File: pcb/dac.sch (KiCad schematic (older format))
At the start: 68 parts, among them U7 MAX5853ETL-T, U8 TLV3542IDR

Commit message: clean up ERC, more DFT stuff, started sigma delta adc
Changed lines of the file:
@@
 $Descr A4 11693 8268
 encoding utf-8
-Sheet 4 6
+Sheet 4 7
 Title ""
 Date ""
@@
 Connection ~ 10550 900
 Wire Wire Line
-	10550 900  10400 900
+	10550 900  10450 900
 $Comp
 L Connector:TestPoint TP27
@@
 Connection ~ 10550 1750
 Wire Wire Line
-	10550 1750 10400 1750
+	10550 1750 10450 1750
 $Comp
 L Connector:TestPoint TP28
@@
 Connection ~ 10550 2600
 Wire Wire Line
-	10550 2600 10400 2600
+	10550 2600 10450 2600
 $Comp
 L Connector:TestPoint TP22
@@
 Wire Bus Line
 	2450 2250 2450 3350
+$Comp
+L power:PWR_FLAG #FLG0106
+U 1 1 604F650D
+P 10450 2600
+F 0 "#FLG0106" H 10450 2675 50  0001 C CNN
+F 1 "PWR_FLAG" H 10450 2773 50  0000 C CNN
+F 2 "" H 10450 2600 50  0001 C CNN
+F 3 "~" H 10450 2600 50  0001 C CNN
+	1    10450 2600
+	1    0    0    -1
+$EndComp
+Connection ~ 10450 2600
+Wire Wire Line
+	10450 2600 10400 2600
+$Comp
+L power:PWR_FLAG #FLG0107
+U 1 1 604F7845
+P 10450 1750
+F 0 "#FLG0107" H 10450 1825 50  0001 C CNN
+F 1 "PWR_FLAG" H 10450 1923 50  0000 C CNN
+F 2 "" H 10450 1750 50  0001 C CNN
+F 3 "~" H 10450 1750 50  0001 C CNN
+	1    10450 1750
+	1    0    0    -1
+$EndComp
+Connection ~ 10450 1750
+Wire Wire Line
+	10450 1750 10400 1750
+$Comp
+L power:PWR_FLAG #FLG0108
+U 1 1 604F7E56
+P 10450 900
+F 0 "#FLG0108" H 10450 975 50  0001 C CNN
+F 1 "PWR_FLAG" H 10450 1073 50  0000 C CNN
+F 2 "" H 10450 900 50  0001 C CNN
+F 3 "~" H 10450 900 50  0001 C CNN
+	1    10450 900
+	1    0    0    -1
+$EndComp
+Connection ~ 10450 900
+Wire Wire Line
+	10450 900  10400 900
 $EndSCHEMATC

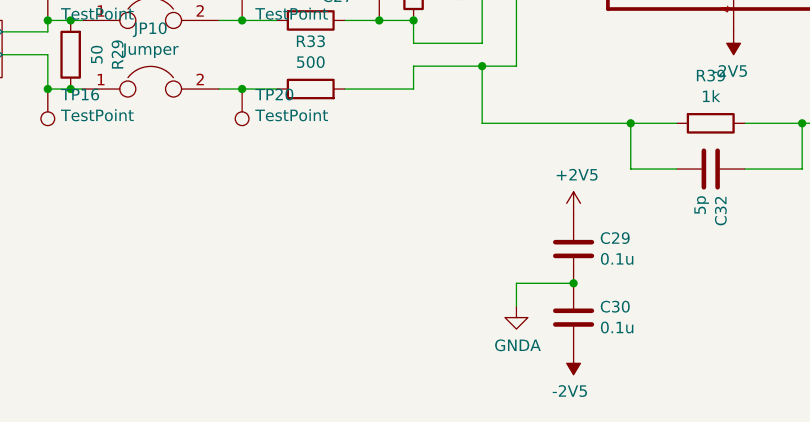
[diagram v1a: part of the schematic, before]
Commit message: add ext LO connectors, more decoupling
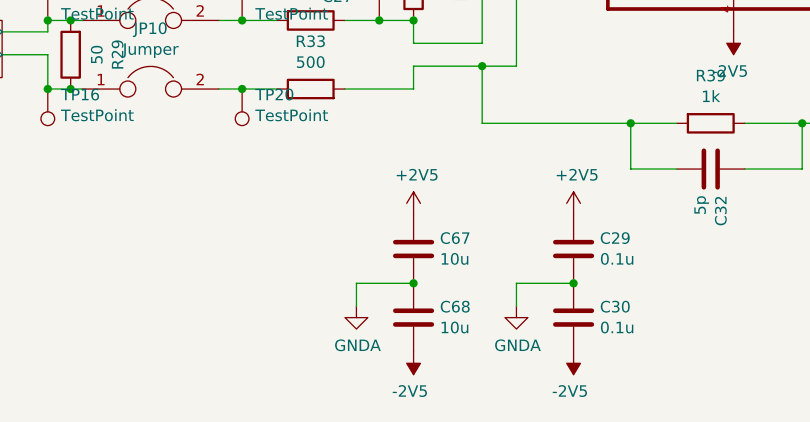
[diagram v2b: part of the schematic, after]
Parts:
- added C67, C68: 10u, symbol Device:C
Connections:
- net +2V5: now also C67.1
- net -2V5: now also C68.2
- net GNDA: now also C67.2, C68.1
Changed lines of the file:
@@
 	1    0    0    -1
 $EndComp
-Wire Bus Line
-	5450 3350 5450 3600
-Wire Bus Line
-	2450 1250 2450 2150
-Wire Bus Line
-	2450 2250 2450 3350
 $Comp
 L power:PWR_FLAG #FLG0106
@@
 Wire Wire Line
 	10450 900  10400 900
+$Comp
+L Device:C C?
+U 1 1 5FC0CF52
+P 5500 7150
+AR Path="/5FC0CF52" Ref="C?"  Part="1"
+AR Path="/5FB3742F/5FC0CF52" Ref="C67"  Part="1"
+F 0 "C67" H 5615 7196 50  0000 L CNN
+F 1 "10u" H 5615 7105 50  0000 L CNN
+F 2 "" H 5538 7000 50  0001 C CNN
+F 3 "~" H 5500 7150 50  0001 C CNN
+	1    5500 7150
+	1    0    0    -1
+$EndComp
+$Comp
+L Device:C C?
+U 1 1 5FC0CF58
+P 5500 7450
+AR Path="/5FC0CF58" Ref="C?"  Part="1"
+AR Path="/5FB3742F/5FC0CF58" Ref="C68"  Part="1"
+F 0 "C68" H 5615 7496 50  0000 L CNN
+F 1 "10u" H 5615 7405 50  0000 L CNN
+F 2 "" H 5538 7300 50  0001 C CNN
+F 3 "~" H 5500 7450 50  0001 C CNN
+	1    5500 7450
+	1    0    0    -1
+$EndComp
+$Comp
+L power:-2V5 #PWR?
+U 1 1 5FC0CF5E
+P 5500 7600
+AR Path="/5FC0CF5E" Ref="#PWR?"  Part="1"
+AR Path="/5FB3742F/5FC0CF5E" Ref="#PWR026"  Part="1"
+F 0 "#PWR026" H 5500 7700 50  0001 C CNN
+F 1 "-2V5" H 5515 7773 50  0000 C CNN
+F 2 "" H 5500 7600 50  0001 C CNN
+F 3 "" H 5500 7600 50  0001 C CNN
+	1    5500 7600
+	-1   0    0    1
+$EndComp
+$Comp
+L power:+2V5 #PWR025
+U 1 1 5FC0CF64
+P 5500 7000
+F 0 "#PWR025" H 5500 6850 50  0001 C CNN
+F 1 "+2V5" H 5515 7173 50  0000 C CNN
+F 2 "" H 5500 7000 50  0001 C CNN
+F 3 "" H 5500 7000 50  0001 C CNN
+	1    5500 7000
+	1    0    0    -1
+$EndComp
+$Comp
+L power:GNDA #PWR024
+U 1 1 5FC0CF6A
+P 5250 7400
+F 0 "#PWR024" H 5250 7150 50  0001 C CNN
+F 1 "GNDA" H 5255 7227 50  0000 C CNN
+F 2 "" H 5250 7400 50  0001 C CNN
+F 3 "" H 5250 7400 50  0001 C CNN
+	1    5250 7400
+	1    0    0    -1
+$EndComp
+Wire Wire Line
+	5250 7400 5250 7300
+Wire Wire Line
+	5250 7300 5500 7300
+Connection ~ 5500 7300
+Wire Bus Line
+	5450 3350 5450 3600
+Wire Bus Line
+	2450 1250 2450 2150
+Wire Bus Line
+	2450 2250 2450 3350
 $EndSCHEMATC

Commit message: started assigning footprints
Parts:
- C26, C27, C28, C29, C30, C31, C32, C33, C34, C35, C36, C37, C38, C67, C68: footprint (none) -> Capacitor_SMD:C_0805_2012Metric_Pad1.15x1.40mm_HandSolder
- R24, R25, R26, R27, R28, R29, R30, R31, R32, R33, R34, R35, R36, R37, R38, R39, R40, R41: footprint (none) -> Resistor_SMD:R_0805_2012Metric_Pad1.20x1.40mm_HandSolder
- U7: footprint 21-0141I_T4066-2 -> (none)
- U8: footprint SOIC127P599X175-8N -> (none)
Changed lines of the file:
@@
 F 0 "U8" H 6850 6270 50  0000 C CNN
 F 1 "TLV3542IDR" H 6850 6179 50  0000 C CNN
-F 2 "SOIC127P599X175-8N" H 6850 5600 50  0001 L BNN
+F 2 "" H 6850 5600 50  0001 L BNN
 F 3 "" H 6850 5600 50  0001 C CNN
 	1    6850 5600
@@
 F 0 "R25" V 1357 5200 50  0000 C CNN
 F 1 "25" V 1266 5200 50  0000 C CNN
-F 2 "" V 1080 5200 50  0001 C CNN
+F 2 "Resistor_SMD:R_0805_2012Metric_Pad1.20x1.40mm_HandSolder" V 1080 5200 50  0001 C CNN
 F 3 "~" H 1150 5200 50  0001 C CNN
 	1    1150 5200
@@
 F 0 "R24" V 943 4600 50  0000 C CNN
 F 1 "25" V 1034 4600 50  0000 C CNN
-F 2 "" V 1080 4600 50  0001 C CNN
+F 2 "Resistor_SMD:R_0805_2012Metric_Pad1.20x1.40mm_HandSolder" V 1080 4600 50  0001 C CNN
 F 3 "~" H 1150 4600 50  0001 C CNN
 	1    1150 4600
@@
 F 0 "R31" V 5257 5050 50  0000 C CNN
 F 1 "500" V 5166 5050 50  0000 C CNN
-F 2 "" V 4980 5050 50  0001 C CNN
+F 2 "Resistor_SMD:R_0805_2012Metric_Pad1.20x1.40mm_HandSolder" V 4980 5050 50  0001 C CNN
 F 3 "~" H 5050 5050 50  0001 C CNN
 	1    5050 5050
@@
 F 0 "R30" V 4843 4750 50  0000 C CNN
 F 1 "500" V 4934 4750 50  0000 C CNN
-F 2 "" V 4980 4750 50  0001 C CNN
+F 2 "Resistor_SMD:R_0805_2012Metric_Pad1.20x1.40mm_HandSolder" V 4980 4750 50  0001 C CNN
 F 3 "~" H 5050 4750 50  0001 C CNN
 	1    5050 4750
@@
 F 0 "R38" V 6593 4600 50  0000 C CNN
 F 1 "1k" V 6684 4600 50  0000 C CNN
-F 2 "" V 6730 4600 50  0001 C CNN
+F 2 "Resistor_SMD:R_0805_2012Metric_Pad1.20x1.40mm_HandSolder" V 6730 4600 50  0001 C CNN
 F 3 "~" H 6800 4600 50  0001 C CNN
 	1    6800 4600
@@
 F 0 "R34" V 5293 4600 50  0000 C CNN
 F 1 "1k" V 5384 4600 50  0000 C CNN
-F 2 "" V 5430 4600 50  0001 C CNN
+F 2 "Resistor_SMD:R_0805_2012Metric_Pad1.20x1.40mm_HandSolder" V 5430 4600 50  0001 C CNN
 F 3 "~" H 5500 4600 50  0001 C CNN
 	1    5500 4600
@@
 F 0 "R27" V 1357 6600 50  0000 C CNN
 F 1 "25" V 1266 6600 50  0000 C CNN
-F 2 "" V 1080 6600 50  0001 C CNN
+F 2 "Resistor_SMD:R_0805_2012Metric_Pad1.20x1.40mm_HandSolder" V 1080 6600 50  0001 C CNN
 F 3 "~" H 1150 6600 50  0001 C CNN
 	1    1150 6600
@@
 F 0 "R26" V 943 6000 50  0000 C CNN
 F 1 "25" V 1034 6000 50  0000 C CNN
-F 2 "" V 1080 6000 50  0001 C CNN
+F 2 "Resistor_SMD:R_0805_2012Metric_Pad1.20x1.40mm_HandSolder" V 1080 6000 50  0001 C CNN
 F 3 "~" H 1150 6000 50  0001 C CNN
 	1    1150 6000
@@
 F 0 "R33" V 5257 6450 50  0000 C CNN
 F 1 "500" V 5166 6450 50  0000 C CNN
-F 2 "" V 4980 6450 50  0001 C CNN
+F 2 "Resistor_SMD:R_0805_2012Metric_Pad1.20x1.40mm_HandSolder" V 4980 6450 50  0001 C CNN
 F 3 "~" H 5050 6450 50  0001 C CNN
 	1    5050 6450
@@
 F 0 "R32" V 4843 6150 50  0000 C CNN
 F 1 "500" V 4934 6150 50  0000 C CNN
-F 2 "" V 4980 6150 50  0001 C CNN
+F 2 "Resistor_SMD:R_0805_2012Metric_Pad1.20x1.40mm_HandSolder" V 4980 6150 50  0001 C CNN
 F 3 "~" H 5050 6150 50  0001 C CNN
 	1    5050 6150
@@
 F 0 "R35" V 5293 6000 50  0000 C CNN
 F 1 "1k" V 5384 6000 50  0000 C CNN
-F 2 "" V 5430 6000 50  0001 C CNN
+F 2 "Resistor_SMD:R_0805_2012Metric_Pad1.20x1.40mm_HandSolder" V 5430 6000 50  0001 C CNN
 F 3 "~" H 5500 6000 50  0001 C CNN
 	1    5500 6000
@@
 F 0 "R39" V 6593 6600 50  0000 C CNN
 F 1 "1k" V 6684 6600 50  0000 C CNN
-F 2 "" V 6730 6600 50  0001 C CNN
+F 2 "Resistor_SMD:R_0805_2012Metric_Pad1.20x1.40mm_HandSolder" V 6730 6600 50  0001 C CNN
 F 3 "~" H 6800 6600 50  0001 C CNN
 	1    6800 6600
@@
 F 0 "C32" H 6915 6846 50  0000 L CNN
 F 1 "5p" H 6915 6755 50  0000 L CNN
-F 2 "" H 6838 6650 50  0001 C CNN
+F 2 "Capacitor_SMD:C_0805_2012Metric_Pad1.15x1.40mm_HandSolder" H 6838 6650 50  0001 C CNN
 F 3 "~" H 6800 6800 50  0001 C CNN
 	1    6800 6800
@@
 F 0 "C31" H 6915 4196 50  0000 L CNN
 F 1 "5p" H 6915 4105 50  0000 L CNN
-F 2 "" H 6838 4000 50  0001 C CNN
+F 2 "Capacitor_SMD:C_0805_2012Metric_Pad1.15x1.40mm_HandSolder" H 6838 4000 50  0001 C CNN
 F 3 "~" H 6800 4150 50  0001 C CNN
 	1    6800 4150
@@
 F 0 "C26" H 5465 4646 50  0000 L CNN
 F 1 "5p" H 5465 4555 50  0000 L CNN
-F 2 "" H 5388 4450 50  0001 C CNN
+F 2 "Capacitor_SMD:C_0805_2012Metric_Pad1.15x1.40mm_HandSolder" H 5388 4450 50  0001 C CNN
 F 3 "~" H 5350 4600 50  0001 C CNN
 	1    5350 4600
@@
 F 0 "C27" H 5465 6046 50  0000 L CNN
 F 1 "5p" H 5465 5955 50  0000 L CNN
-F 2 "" H 5388 5850 50  0001 C CNN
+F 2 "Capacitor_SMD:C_0805_2012Metric_Pad1.15x1.40mm_HandSolder" H 5388 5850 50  0001 C CNN
 F 3 "~" H 5350 6000 50  0001 C CNN
 	1    5350 6000
@@
 F 0 "R28" V 3793 4900 50  0000 C CNN
 F 1 "50" V 3884 4900 50  0000 C CNN
-F 2 "" V 3930 4900 50  0001 C CNN
+F 2 "Resistor_SMD:R_0805_2012Metric_Pad1.20x1.40mm_HandSolder" V 3930 4900 50  0001 C CNN
 F 3 "~" H 4000 4900 50  0001 C CNN
 	1    4000 4900
@@
 F 0 "R29" V 3793 6300 50  0000 C CNN
 F 1 "50" V 3884 6300 50  0000 C CNN
-F 2 "" V 3930 6300 50  0001 C CNN
+F 2 "Resistor_SMD:R_0805_2012Metric_Pad1.20x1.40mm_HandSolder" V 3930 6300 50  0001 C CNN
 F 3 "~" H 4000 6300 50  0001 C CNN
 	1    4000 6300
@@
 F 0 "C33" H 10115 1246 50  0000 L CNN
 F 1 "0.1u" H 10115 1155 50  0000 L CNN
-F 2 "" H 10038 1050 50  0001 C CNN
+F 2 "Capacitor_SMD:C_0805_2012Metric_Pad1.15x1.40mm_HandSolder" H 10038 1050 50  0001 C CNN
 F 3 "~" H 10000 1200 50  0001 C CNN
 	1    10000 1200
@@
 F 0 "C36" H 10515 1246 50  0000 L CNN
 F 1 "10u" H 10515 1155 50  0000 L CNN
-F 2 "" H 10438 1050 50  0001 C CNN
+F 2 "Capacitor_SMD:C_0805_2012Metric_Pad1.15x1.40mm_HandSolder" H 10438 1050 50  0001 C CNN
 F 3 "~" H 10400 1200 50  0001 C CNN
 	1    10400 1200
@@
 F 0 "C34" H 10115 2096 50  0000 L CNN
 F 1 "0.1u" H 10115 2005 50  0000 L CNN
-F 2 "" H 10038 1900 50  0001 C CNN
+F 2 "Capacitor_SMD:C_0805_2012Metric_Pad1.15x1.40mm_HandSolder" H 10038 1900 50  0001 C CNN
 F 3 "~" H 10000 2050 50  0001 C CNN
 	1    10000 2050
@@
 F 0 "C37" H 10515 2096 50  0000 L CNN
 F 1 "10u" H 10515 2005 50  0000 L CNN
-F 2 "" H 10438 1900 50  0001 C CNN
+F 2 "Capacitor_SMD:C_0805_2012Metric_Pad1.15x1.40mm_HandSolder" H 10438 1900 50  0001 C CNN
 F 3 "~" H 10400 2050 50  0001 C CNN
 	1    10400 2050
@@
 F 0 "C35" H 10115 2946 50  0000 L CNN
 F 1 "0.1u" H 10115 2855 50  0000 L CNN
-F 2 "" H 10038 2750 50  0001 C CNN
+F 2 "Capacitor_SMD:C_0805_2012Metric_Pad1.15x1.40mm_HandSolder" H 10038 2750 50  0001 C CNN
 F 3 "~" H 10000 2900 50  0001 C CNN
 	1    10000 2900
@@
 F 0 "C38" H 10515 2946 50  0000 L CNN
 F 1 "10u" H 10515 2855 50  0000 L CNN
-F 2 "" H 10438 2750 50  0001 C CNN
+F 2 "Capacitor_SMD:C_0805_2012Metric_Pad1.15x1.40mm_HandSolder" H 10438 2750 50  0001 C CNN
 F 3 "~" H 10400 2900 50  0001 C CNN
 	1    10400 2900
@@
 F 0 "C29" H 6315 7196 50  0000 L CNN
 F 1 "0.1u" H 6315 7105 50  0000 L CNN
-F 2 "" H 6238 7000 50  0001 C CNN
+F 2 "Capacitor_SMD:C_0805_2012Metric_Pad1.15x1.40mm_HandSolder" H 6238 7000 50  0001 C CNN
 F 3 "~" H 6200 7150 50  0001 C CNN
 	1    6200 7150
@@
 F 0 "C30" H 6315 7496 50  0000 L CNN
 F 1 "0.1u" H 6315 7405 50  0000 L CNN
-F 2 "" H 6238 7300 50  0001 C CNN
+F 2 "Capacitor_SMD:C_0805_2012Metric_Pad1.15x1.40mm_HandSolder" H 6238 7300 50  0001 C CNN
 F 3 "~" H 6200 7450 50  0001 C CNN
 	1    6200 7450
@@
 F 0 "R36" V 6343 2650 50  0000 C CNN
 F 1 "6.8k - optional output termination" V 6434 2650 50  0000 C CNN
-F 2 "" V 6480 2650 50  0001 C CNN
+F 2 "Resistor_SMD:R_0805_2012Metric_Pad1.20x1.40mm_HandSolder" V 6480 2650 50  0001 C CNN
 F 3 "~" H 6550 2650 50  0001 C CNN
 	1    6550 2650
@@
 F 0 "C28" H 6065 2396 50  0000 L CNN
 F 1 "0.1u" H 6065 2305 50  0000 L CNN
-F 2 "" H 5988 2200 50  0001 C CNN
+F 2 "Capacitor_SMD:C_0805_2012Metric_Pad1.15x1.40mm_HandSolder" H 5988 2200 50  0001 C CNN
 F 3 "~" H 5950 2350 50  0001 C CNN
 	1    5950 2350
@@
 F 0 "R37" V 6393 2250 50  0000 C CNN
 F 1 "1.985k" V 6484 2250 50  0000 C CNN
-F 2 "" V 6530 2250 50  0001 C CNN
+F 2 "Resistor_SMD:R_0805_2012Metric_Pad1.20x1.40mm_HandSolder" V 6530 2250 50  0001 C CNN
 F 3 "~" H 6600 2250 50  0001 C CNN
 	1    6600 2250
@@
 F 0 "R40" V 7493 5350 50  0000 C CNN
 F 1 "50" V 7584 5350 50  0000 C CNN
-F 2 "" V 7630 5350 50  0001 C CNN
+F 2 "Resistor_SMD:R_0805_2012Metric_Pad1.20x1.40mm_HandSolder" V 7630 5350 50  0001 C CNN
 F 3 "~" H 7700 5350 50  0001 C CNN
 	1    7700 5350
@@
 F 0 "R41" V 7493 5800 50  0000 C CNN
 F 1 "50" V 7584 5800 50  0000 C CNN
-F 2 "" V 7630 5800 50  0001 C CNN
+F 2 "Resistor_SMD:R_0805_2012Metric_Pad1.20x1.40mm_HandSolder" V 7630 5800 50  0001 C CNN
 F 3 "~" H 7700 5800 50  0001 C CNN
 	1    7700 5800
@@
 F 0 "U7" H 3950 1715 50  0000 C CNN
 F 1 "MAX5853ETL-T" H 3950 1624 50  0000 C CNN
-F 2 "21-0141I_T4066-2" H 2550 1350 50  0001 L BNN
+F 2 "" H 2550 1350 50  0001 L BNN
 F 3 "max5853etlt" H 2550 1350 50  0001 L BNN
 F 4 "MAXIM" H 2550 1350 50  0001 L BNN "Field4"
@@
 F 0 "C67" H 5615 7196 50  0000 L CNN
 F 1 "10u" H 5615 7105 50  0000 L CNN
-F 2 "" H 5538 7000 50  0001 C CNN
+F 2 "Capacitor_SMD:C_0805_2012Metric_Pad1.15x1.40mm_HandSolder" H 5538 7000 50  0001 C CNN
 F 3 "~" H 5500 7150 50  0001 C CNN
 	1    5500 7150
@@
 F 0 "C68" H 5615 7496 50  0000 L CNN
 F 1 "10u" H 5615 7405 50  0000 L CNN
-F 2 "" H 5538 7300 50  0001 C CNN
+F 2 "Capacitor_SMD:C_0805_2012Metric_Pad1.15x1.40mm_HandSolder" H 5538 7300 50  0001 C CNN
 F 3 "~" H 5500 7450 50  0001 C CNN
 	1    5500 7450
